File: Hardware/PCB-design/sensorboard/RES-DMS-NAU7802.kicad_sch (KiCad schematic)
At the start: 43 parts, among them J1 Conn_01x06, J2 straingauge, J3 straingauge, J4 straingauge, J5 straingauge, J6 straingauge, J7 straingauge, J8 straingauge, J9 straingauge, U1 NAU7802-SGI

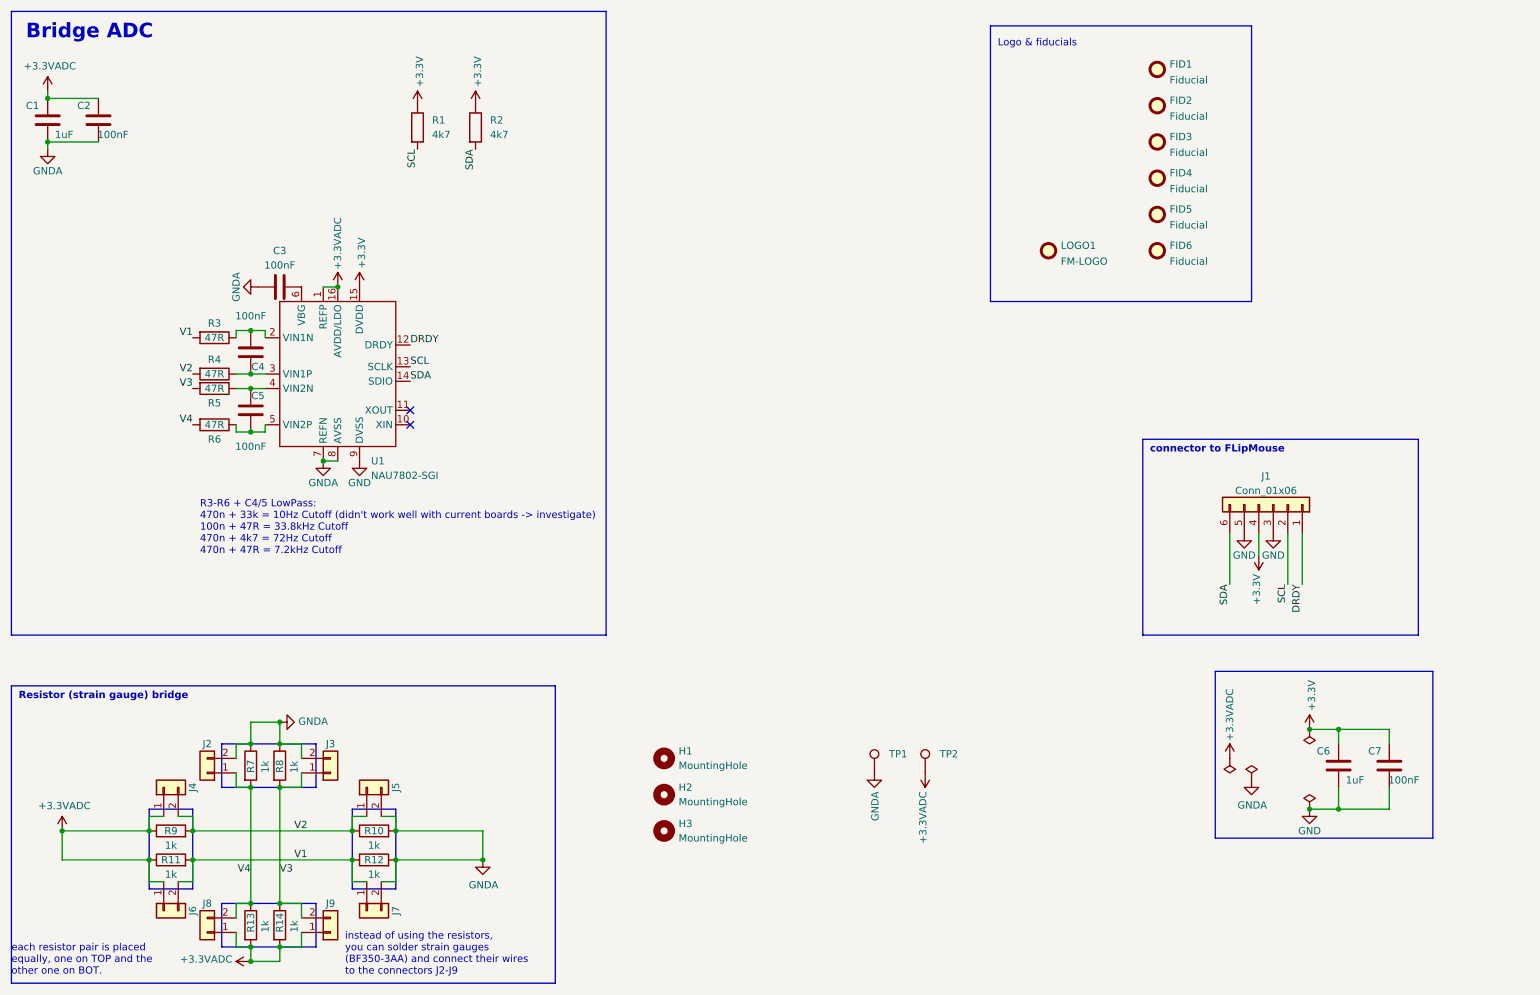
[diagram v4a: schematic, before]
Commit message: Changed to v3.3 layout with DMS & possibility for resistors. Changed to 4 hole design again.
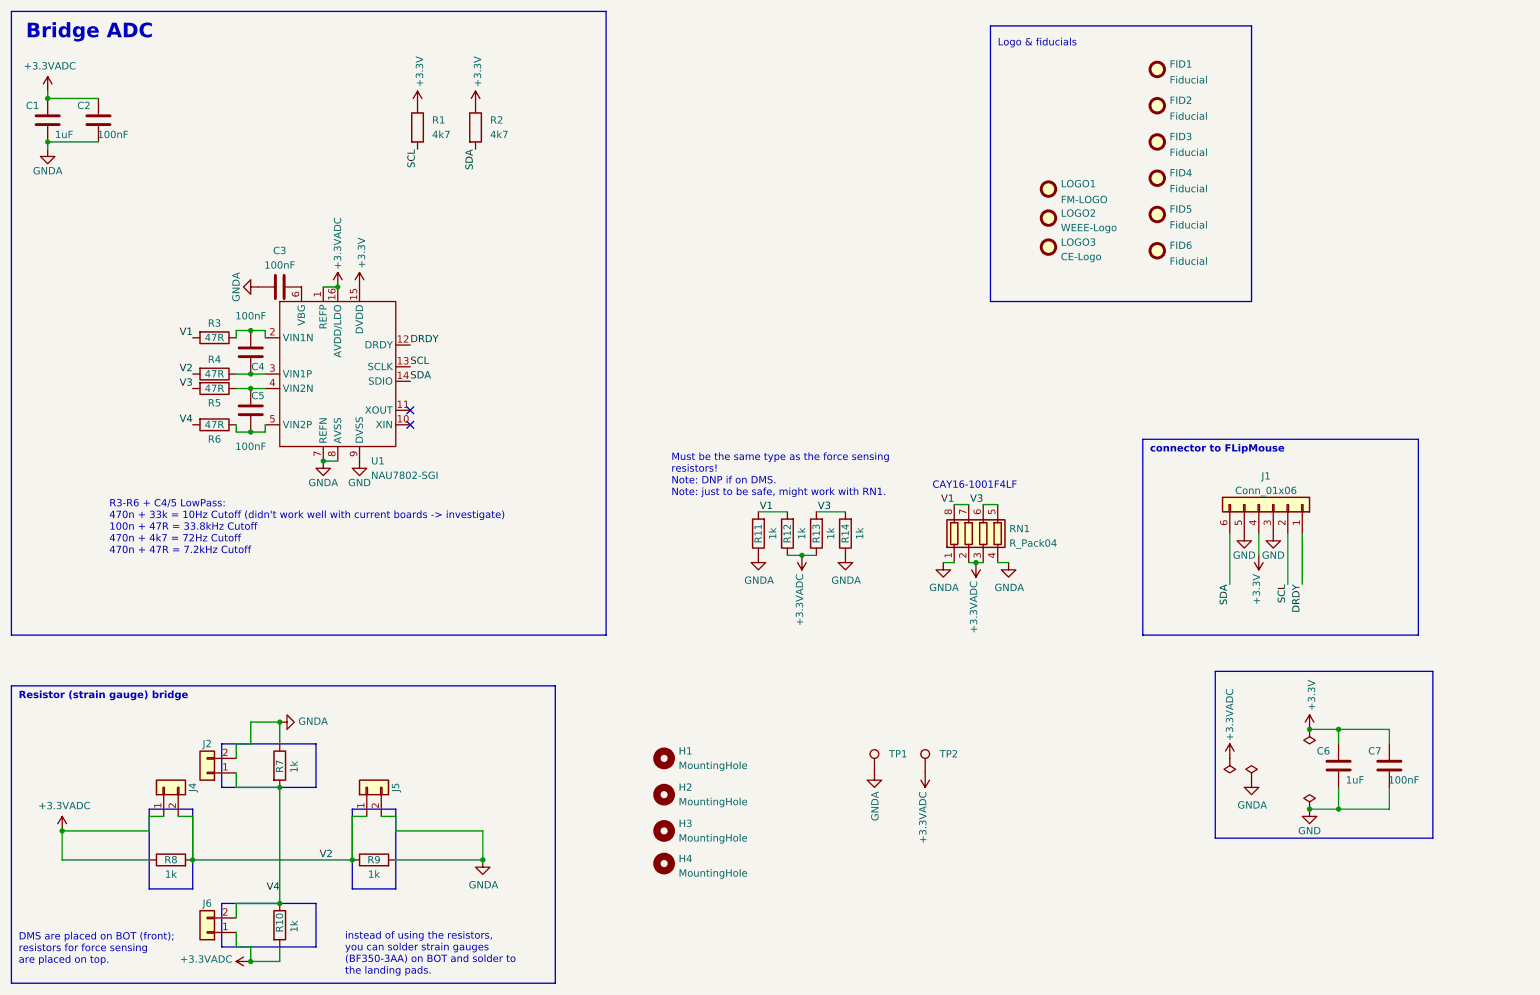
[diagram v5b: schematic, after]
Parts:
- removed J3, J6, J7, J9: straingauge, Project:straingauges, symbol Connector_Generic:Conn_01x02
- removed R10, R7, R9: 1k, Resistor_SMD:R_1206_3216Metric_Pad1.30x1.75mm_HandSolder, symbol Device:R
- added H4: MountingHole, MountingHole:MountingHole_2.2mm_M2_DIN965, symbol Mechanical:MountingHole
- added LOGO2: WEEE-Logo, Symbol:WEEE-Logo_4.2x6mm_SilkScreen, symbol Mechanical:Fiducial
- added LOGO3: CE-Logo, Symbol:CE-Logo_8.5x6mm_SilkScreen, symbol Mechanical:Fiducial
- added R11, R12, R14: 1k, Resistor_SMD:R_1206_3216Metric, symbol Device:R
- added RN1: R_Pack04, Resistor_SMD:R_Array_Convex_4x1206, symbol Device:R_Pack04
- C1, C2, C3, C4, C5, C6, C7: footprint Capacitor_SMD:C_0603_1608Metric_Pad1.08x0.95mm_HandSolder -> Capacitor_SMD:C_0603_1608Metric
- FID1, FID2, FID3, FID4, FID5, FID6, LOGO1: now left out of the parts list
- J1: footprint Connector_PinHeader_1.27mm:PinHeader_1x06_P1.27mm_Vertical -> Project:690367280676
- R1, R2, R3, R4, R5, R6: footprint Resistor_SMD:R_0603_1608Metric_Pad0.98x0.95mm_HandSolder -> Resistor_SMD:R_0603_1608Metric
- R10: renamed from R14; footprint Resistor_SMD:R_1206_3216Metric_Pad1.30x1.75mm_HandSolder -> Resistor_SMD:R_1206_3216Metric
- R13: footprint Resistor_SMD:R_1206_3216Metric_Pad1.30x1.75mm_HandSolder -> Resistor_SMD:R_1206_3216Metric
- R7: renamed from R8; footprint Resistor_SMD:R_1206_3216Metric_Pad1.30x1.75mm_HandSolder -> Resistor_SMD:R_1206_3216Metric
- R8: renamed from R11; footprint Resistor_SMD:R_1206_3216Metric_Pad1.30x1.75mm_HandSolder -> Resistor_SMD:R_1206_3216Metric
- R9: renamed from R12; footprint Resistor_SMD:R_1206_3216Metric_Pad1.30x1.75mm_HandSolder -> Resistor_SMD:R_1206_3216Metric
- renumbered J8 to J6
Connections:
- net +3.3VADC: now also R13.1, R12.1, RN1.2 (R2.1), RN1.3 (R3.1); no longer R13.2
- net GNDA: now also R11.1, R14.1, RN1.1 (R1.1), RN1.4 (R4.1)
- net V1: now also R11.2, R12.2, RN1.7 (R2.2), RN1.8 (R1.2); no longer R8.2, R9.1
- net V2: now also R8.2, R9.1
- net V3: now also R13.2, R14.2, RN1.5 (R4.2), RN1.6 (R3.2); no longer R10.1, R7.2
- net V4: now also R10.1, R7.2; no longer R13.1
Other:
- note added: "CAY16-1001F4LF"
- note added: "DMS are placed on BOT (front); resistors for force sensing are placed on top."
- note added: "Must be the same type as the force sensing resistors! Note: DNP if on DMS. Note: just to be safe, might work with RN1."
- note added: "instead of using the resistors, you can solder strain gauges (BF350-3AA) on BOT and solder to the landing pads."
- note removed: "each resistor pair is placed equally, one on TOP and the other one on BOT."
- note removed: "instead of using the resistors, you can solder strain gauges (BF350-3AA) and connect their wires to the connectors J2-J9"
- moved on the sheet: LOGO1

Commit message: Changed resistor network footprint, was wrong.
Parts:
- RN1: footprint Resistor_SMD:R_Array_Convex_4x1206 -> Resistor_SMD:R_Array_Convex_4x0603
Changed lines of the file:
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@@
       (effects (font (size 1.27 1.27)) (justify left))
     )
-    (property "Footprint" "Resistor_SMD:R_Array_Convex_4x1206" (id 2) (at 207.645 107.95 90)
+    (property "Footprint" "Resistor_SMD:R_Array_Convex_4x0603" (id 2) (at 207.645 107.95 90)
       (effects (font (size 1.27 1.27)) hide)
     )
@@
     )
     (path "/e585351b-5699-4104-99ac-e99731ac32b5"
-      (reference "RN1") (unit 1) (value "R_Pack04") (footprint "Resistor_SMD:R_Array_Convex_4x1206")
+      (reference "RN1") (unit 1) (value "R_Pack04") (footprint "Resistor_SMD:R_Array_Convex_4x0603")
     )
     (path "/479d2297-e59e-40ec-8a75-d08e515c11dd"

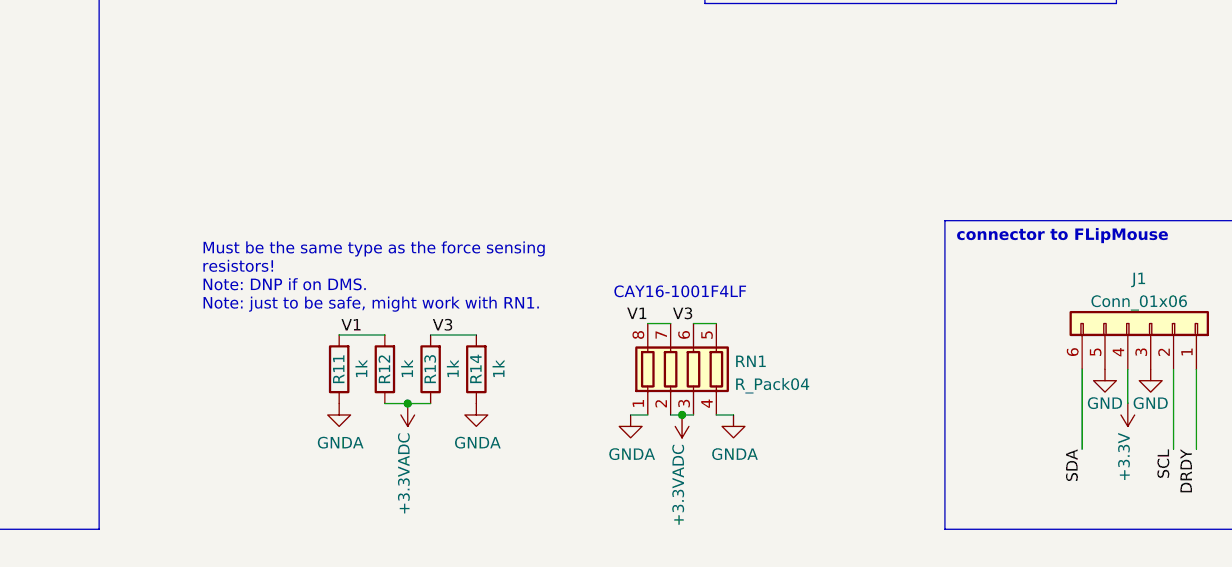
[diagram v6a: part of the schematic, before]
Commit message: Changed resistor values of half bridge (not sensing; should be resistor network)
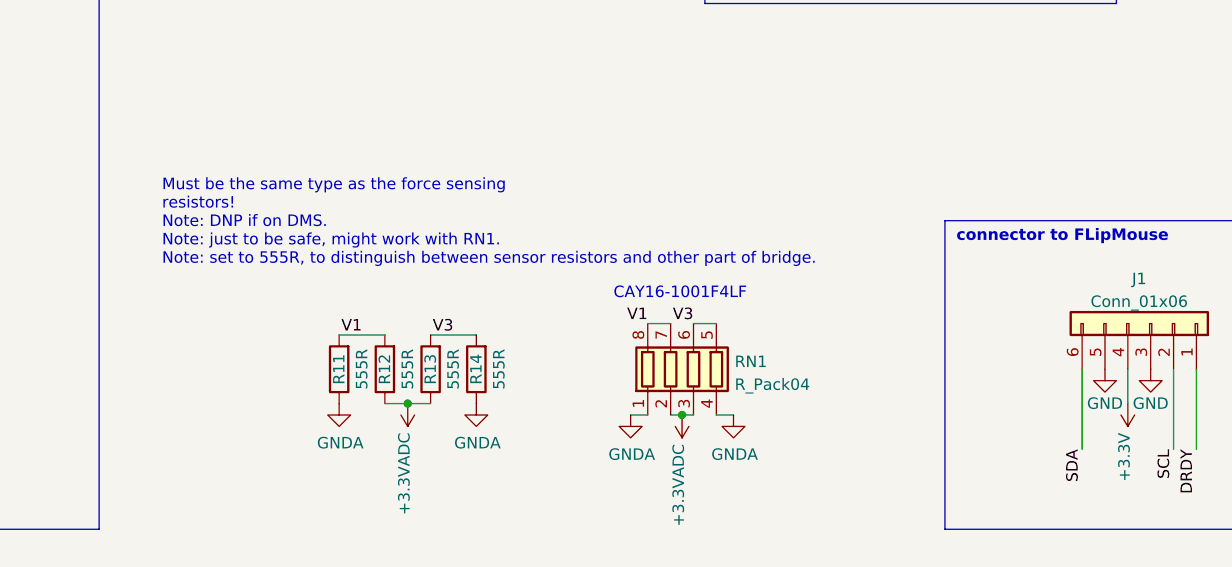
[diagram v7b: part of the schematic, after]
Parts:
- R11, R12, R13, R14: value 1k -> 555R
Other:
- note added: "Must be the same type as the force sensing resistors! Note: DNP if on DMS. Note: just to be safe, might work with RN1. Note: set to 555R, to distinguish between sensor resistors and other part of bridge."
- note removed: "Must be the same type as the force sensing resistors! Note: DNP if on DMS. Note: just to be safe, might work with RN1."
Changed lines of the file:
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@@
     (effects (font (size 1.27 1.27)) (justify left bottom))
   )
-  (text "Must be the same type as the force sensing\nresistors!\nNote: DNP if on DMS.\nNote: just to be safe, might work with RN1."
-    (at 146.05 101.6 0)
+  (text "Must be the same type as the force sensing\nresistors!\nNote: DNP if on DMS.\nNote: just to be safe, might work with RN1.\nNote: set to 555R, to distinguish between sensor resistors and other part of bridge."
+    (at 141.605 96.52 0)
     (effects (font (size 1.27 1.27)) (justify left bottom))
   )
@@
     (in_bom yes) (on_board yes)
     (property "Reference" "R14" (id 0) (at 176.53 107.95 90))
-    (property "Value" "1k" (id 1) (at 179.07 107.95 90))
+    (property "Value" "555R" (id 1) (at 179.07 107.95 90))
     (property "Footprint" "Resistor_SMD:R_1206_3216Metric" (id 2) (at 178.308 107.95 90)
       (effects (font (size 1.27 1.27)) hide)
@@
     (in_bom yes) (on_board yes)
     (property "Reference" "R13" (id 0) (at 171.45 107.95 90))
-    (property "Value" "1k" (id 1) (at 173.99 107.95 90))
+    (property "Value" "555R" (id 1) (at 173.99 107.95 90))
     (property "Footprint" "Resistor_SMD:R_1206_3216Metric" (id 2) (at 173.228 107.95 90)
       (effects (font (size 1.27 1.27)) hide)
@@
     (in_bom yes) (on_board yes)
     (property "Reference" "R11" (id 0) (at 161.29 107.95 90))
-    (property "Value" "1k" (id 1) (at 163.83 107.95 90))
+    (property "Value" "555R" (id 1) (at 163.83 107.95 90))
     (property "Footprint" "Resistor_SMD:R_1206_3216Metric" (id 2) (at 163.068 107.95 90)
       (effects (font (size 1.27 1.27)) hide)
@@
     (in_bom yes) (on_board yes)
     (property "Reference" "R12" (id 0) (at 166.37 107.95 90))
-    (property "Value" "1k" (id 1) (at 168.91 107.95 90))
+    (property "Value" "555R" (id 1) (at 168.91 107.95 90))
     (property "Footprint" "Resistor_SMD:R_1206_3216Metric" (id 2) (at 168.148 107.95 90)
       (effects (font (size 1.27 1.27)) hide)
@@
     )
     (path "/75bc358e-cfd4-4683-9983-e89c2e96b124"
-      (reference "R11") (unit 1) (value "1k") (footprint "Resistor_SMD:R_1206_3216Metric")
+      (reference "R11") (unit 1) (value "555R") (footprint "Resistor_SMD:R_1206_3216Metric")
     )
     (path "/b50bcc1f-0c0c-4c40-9ffe-e9cc6a509b9e"
-      (reference "R12") (unit 1) (value "1k") (footprint "Resistor_SMD:R_1206_3216Metric")
+      (reference "R12") (unit 1) (value "555R") (footprint "Resistor_SMD:R_1206_3216Metric")
     )
     (path "/1c410388-6dbc-4d7f-92bb-c866584eba47"
-      (reference "R13") (unit 1) (value "1k") (footprint "Resistor_SMD:R_1206_3216Metric")
+      (reference "R13") (unit 1) (value "555R") (footprint "Resistor_SMD:R_1206_3216Metric")
     )
     (path "/106b48ce-c343-4bc1-a966-95d5a5c1ee63"
-      (reference "R14") (unit 1) (value "1k") (footprint "Resistor_SMD:R_1206_3216Metric")
+      (reference "R14") (unit 1) (value "555R") (footprint "Resistor_SMD:R_1206_3216Metric")
     )
     (path "/e585351b-5699-4104-99ac-e99731ac32b5"
